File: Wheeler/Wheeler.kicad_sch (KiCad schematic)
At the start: 20 parts, among them J1 USB_C_Receptacle_USB2.0_16P, J2 POWER_INPUT, J3 MOTOR_A_OUTPUT, J4 MOTOR_B_OUTPUT, J5 MOTOR_C_OUTPUT, J6 MOTOR_D_OUTPUT, U1 L293D, U2 L293D, U3 ATmega328P-P, U4 CH340G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

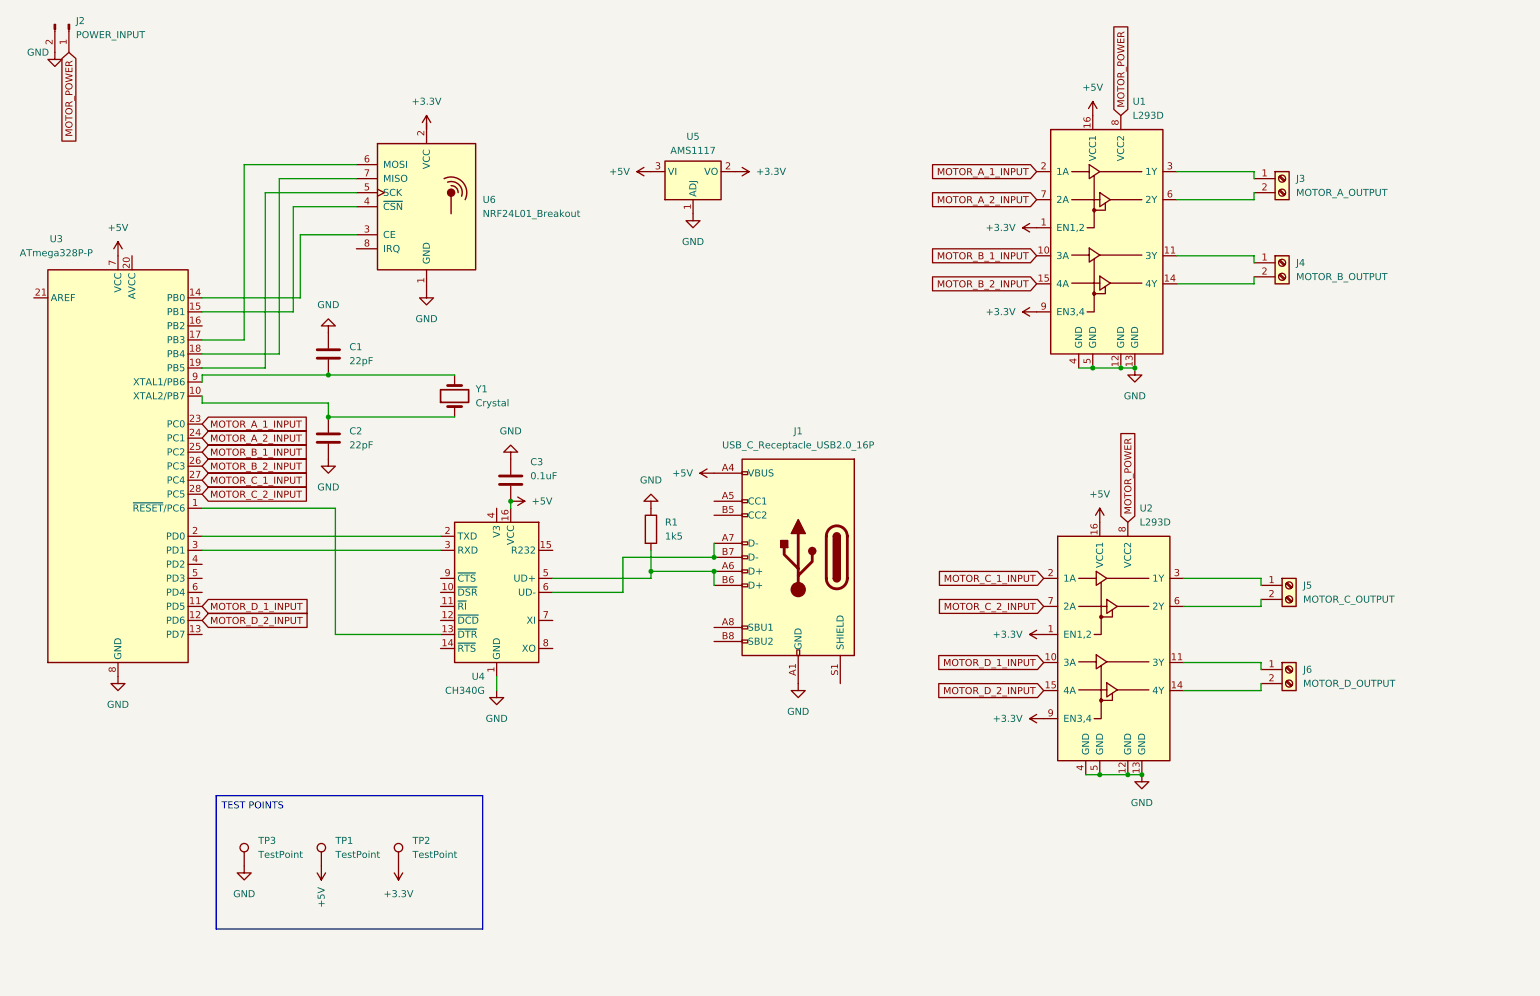
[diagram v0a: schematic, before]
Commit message: Migrated to ESP32 and BLE
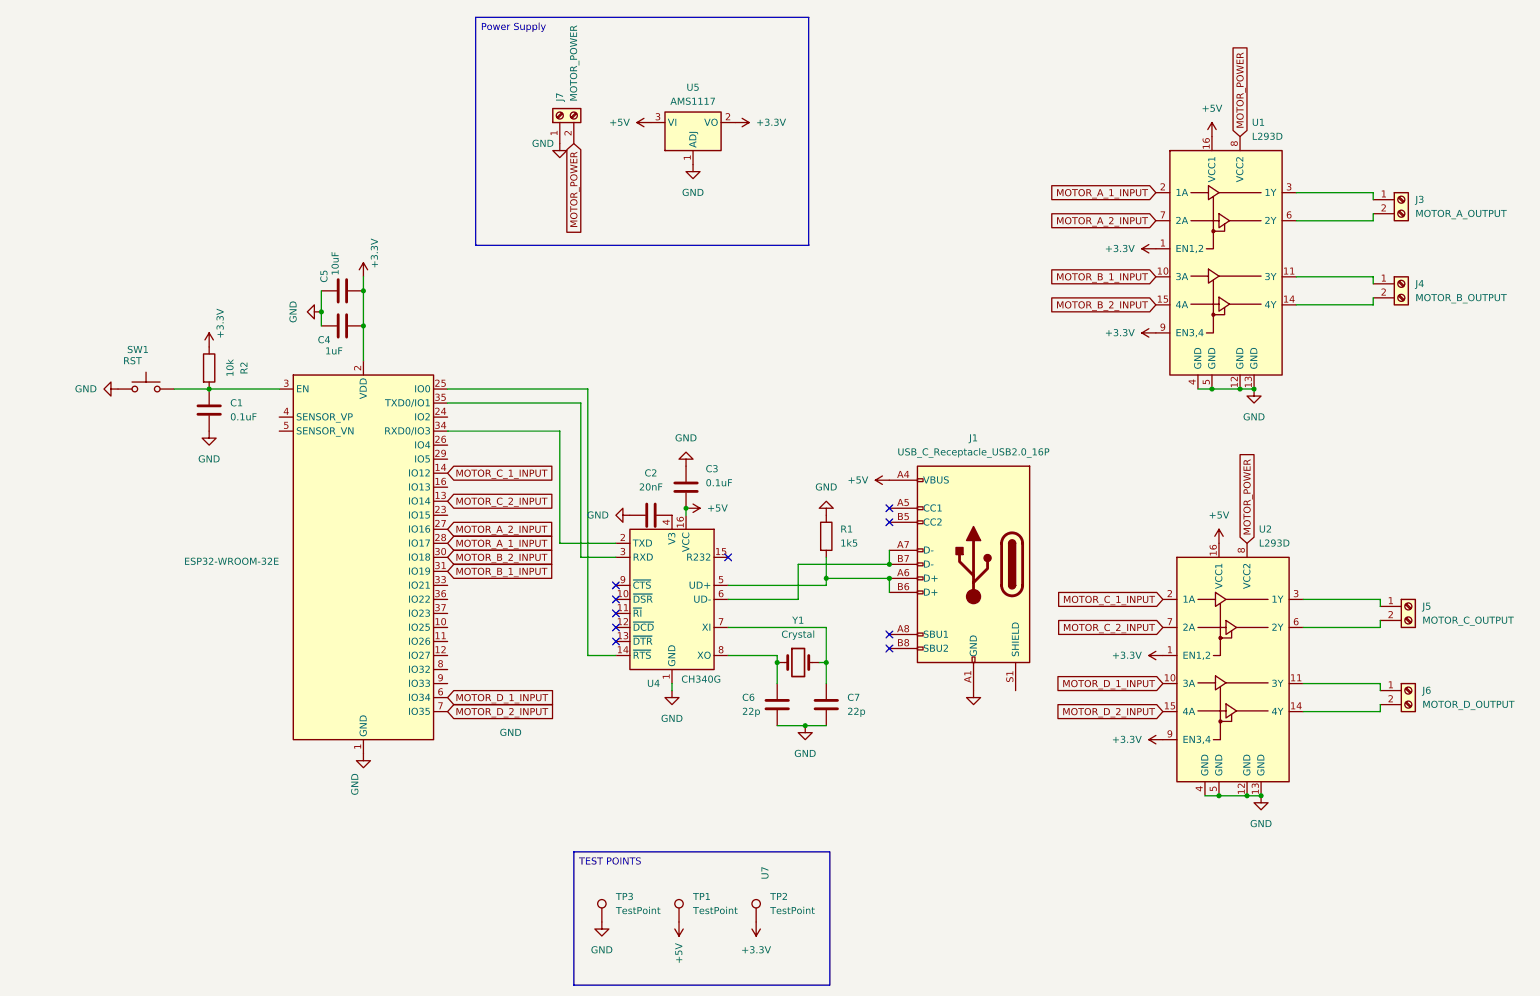
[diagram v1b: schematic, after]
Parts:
- removed J2: POWER_INPUT, Connector_JST:JST_XH_B2B-XH-A_1x02_P2.50mm_Vertical, symbol Connector:Conn_01x02_Pin
- removed U3: ATmega328P-P, Package_DIP:DIP-28_W7.62mm_Socket, symbol MCU_Microchip_ATmega:ATmega328P-P
- removed U6: NRF24L01_Breakout, RF_Module:nRF24L01_Breakout, symbol RF:NRF24L01_Breakout
- added C4: 1uF, Capacitor_SMD:C_0805_2012Metric, symbol Device:C
- added C5: 10uF, Capacitor_SMD:C_0805_2012Metric, symbol Device:C
- added C6, C7: 22p, Capacitor_SMD:C_0805_2012Metric, symbol Device:C
- added J7: MOTOR_POWER, TerminalBlock:TerminalBlock_Xinya_XY308-2.54-2P_1x02_P2.54mm_Horizontal, symbol Connector:Screw_Terminal_01x02
- added R2: 10k, Resistor_SMD:R_0805_2012Metric, symbol Device:R
- added SW1: RST, symbol Switch:SW_Push
- added U7: ESP32-WROOM-32E, RF_Module:ESP32-WROOM-32D, symbol RF_Module:ESP32-WROOM-32E
- C1: value 22pF -> 0.1uF; footprint (none) -> Capacitor_SMD:C_0805_2012Metric
- C2: value 22pF -> 20nF; footprint (none) -> Capacitor_SMD:C_0805_2012Metric
- C3: footprint (none) -> Capacitor_SMD:C_0805_2012Metric
- R1: footprint (none) -> Resistor_SMD:R_0805_2012Metric
- TP2, TP3: footprint (none) -> Connector_Pin:Pin_D0.7mm_L6.5mm_W1.8mm_FlatFork
- Y1: footprint (none) -> Crystal:Crystal_HC49-4H_Vertical
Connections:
- net +3.3V: now also C4.1, C5.1, R2.1, U7.2 (VDD)
- net GND: now also C1.2, C4.2, C5.2, C6.2, C7.2, J7.1 (Pin_1), SW1.1, U7.1 (GND), U7.15 (GND), U7.38 (GND), U7.39 (GND); no longer C1.1
- net MOTOR_A_1_INPUT: now also U7.28 (IO17)
- net MOTOR_A_2_INPUT: now also U7.27 (IO16)
- net MOTOR_B_1_INPUT: now also U7.31 (IO19)
- net MOTOR_B_2_INPUT: now also U7.30 (IO18)
- net MOTOR_C_1_INPUT: now also U7.14 (IO12)
- net MOTOR_C_2_INPUT: now also U7.13 (IO14)
- net MOTOR_D_1_INPUT: now also U7.6 (IO34)
- net MOTOR_D_2_INPUT: now also U7.7 (IO35)
- net MOTOR_POWER: now also J7.2 (Pin_2)
- net at Y1.2: now also U4.7 (XI), C7.1; no longer C1.2
- net at C2.1: now also U4.4 (V3); no longer Y1.1
- net at U4.14 (~{RTS}): now also U7.25 (IO0)
- net at U4.2 (TXD): now also U7.34 (RXD0/IO3)
- net at U4.3 (RXD): now also U7.35 (TXD0/IO1)
- net at U4.8 (XO): now also Y1.1, C6.1
- new net: C1.1, R2.2, SW1.2, U7.3 (EN)
- no-connect marks 0 -> 10
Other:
- moved on the sheet: C3, J1, J3, J4, J5, J6, R1, TP1, TP2, TP3, U1, U2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

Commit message: Questionable Routing
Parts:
- SW1: footprint (none) -> Button_Switch_THT:SW_PUSH_6mm_H4.3mm
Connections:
- no-connect marks 10 -> 11
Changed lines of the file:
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@@
 		(at 121.92 127)
 	)
+	(no_connect
+		(at 194.31 135.89)
+	)
 	(wire
 		(pts
@@
 			)
 		)
-		(property "Footprint" ""
+		(property "Footprint" "Button_Switch_THT:SW_PUSH_6mm_H4.3mm"
 			(at 36.83 76.2 0)
 			(effects
